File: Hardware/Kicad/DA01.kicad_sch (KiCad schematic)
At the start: 27 parts, among them J1 Conn 1x4 pins, J2 Terminal 1x2, J3 Terminal 1x2, J4 Conn 2x3 pins, J5 Terminal 1x8, J6 Terminal 1x2, J7 Conn 1x8 pins, U1 LM7805, U2 6N137, U3 DFPlayerMini

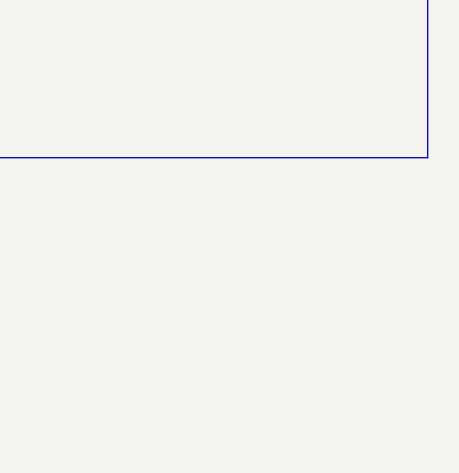
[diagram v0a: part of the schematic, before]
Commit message: Add CTM in cartridge & PCB
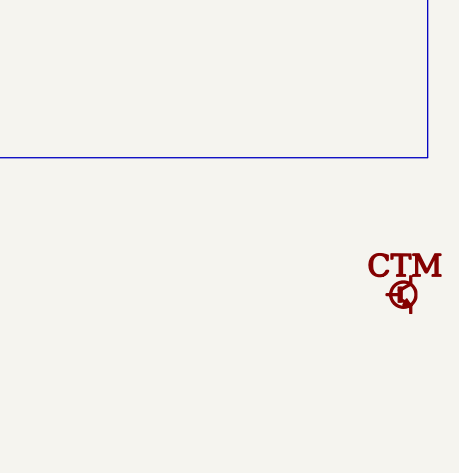
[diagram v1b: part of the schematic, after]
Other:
- company: CTM (ct-modelisme.fr) -> CT-Modélisme (ct-modelisme.fr)
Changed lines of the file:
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@@
   (title_block
     (title "DA01 - Schematic")
-    (date "2022-08-02")
+    (date "2024-02-17")
     (rev "1.1")
-    (company "CTM (ct-modelisme.fr)")
-    (comment 1 "All rights reserved")
+    (company "CT-Modélisme (ct-modelisme.fr)")
+    (comment 1 "Rev 1.1 - 2022-08-02")
   )
   (junction (at 198.12 129.54) (diameter 0) (color 0 0 0 0)
@@
     (pin "4")
   )
+  (symbol (lib_id "CTM:Logo_CTM") (at 276.86 173.99 0) (unit 1)
+    (in_bom yes) (on_board yes) (fields_autoplaced)
+    (property "Reference" "#G?" (id 0) (at 276.86 171.2992 0)
+      (effects (font (size 1.27 1.27)) hide)
+    )
+    (property "Value" "Logo_CTM" (id 1) (at 276.86 176.6808 0)
+      (effects (font (size 1.27 1.27)) hide)
+    )
+    (property "Footprint" "" (id 2) (at 276.86 173.99 0)
+      (effects (font (size 1.27 1.27)) hide)
+    )
+    (property "Datasheet" "" (id 3) (at 276.86 173.99 0)
+      (effects (font (size 1.27 1.27)) hide)
+    )
+  )
   (sheet_instances
     (path "/" (page "1"))
   )
   (symbol_instances
+    (path "/6bafad74-6bf0-496f-9568-2b5173f7a906"
+      (reference "#G?") (unit 1) (value "Logo_CTM") (footprint "")
+    )
     (path "/00000000-0000-0000-0000-000060d5d288"
       (reference "#PWR01") (unit 1) (value "+5V") (footprint "")
